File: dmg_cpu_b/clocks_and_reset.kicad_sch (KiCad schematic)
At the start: 112 parts

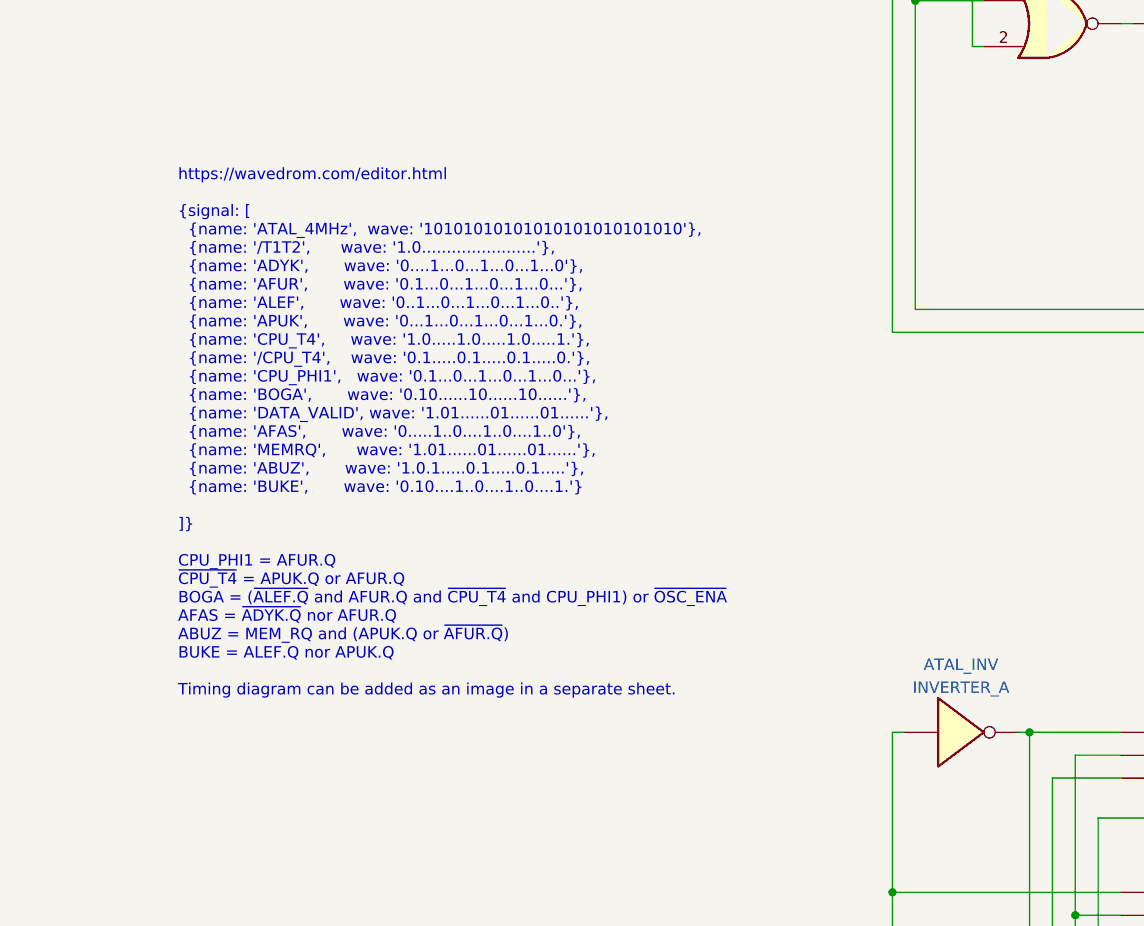
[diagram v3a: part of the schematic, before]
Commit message: Fixed DMA phi2 signal. Notes tidied up, page order modified and draft pdf created for review.
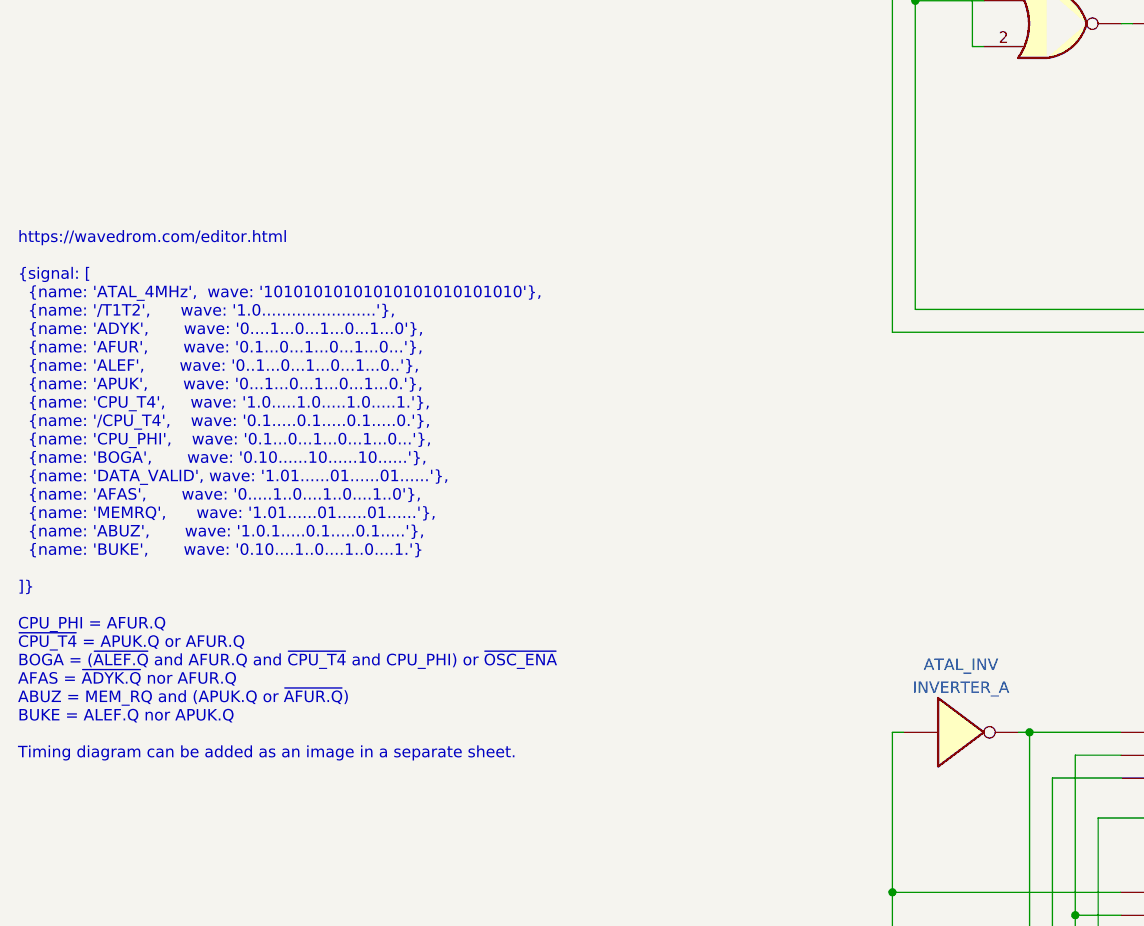
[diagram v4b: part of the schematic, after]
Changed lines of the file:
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@@
   (title_block
     (title "DMG CPU B")
-    (date "2022-05-19")
-    (rev "0")
+    (date "2022-07-08")
+    (rev "0.1")
     (company "CC-BY-SA-4.0 Régis Galland & Michael Singer -- Derived work from Furrtek")
     (comment 1 "https://github.com/msinger/dmg-schematics")
@@
     (effects (font (size 1.27 1.27)) (justify left bottom))
   )
-  (text "https://wavedrom.com/editor.html\n\n{signal: [\n  {name: 'ATAL_4MHz',  wave: '10101010101010101010101010'},\n  {name: '/T1T2',      wave: '1.0.......................'},\n  {name: 'ADYK',       wave: '0....1...0...1...0...1...0'},\n  {name: 'AFUR',       wave: '0.1...0...1...0...1...0...'},\n  {name: 'ALEF',       wave: '0..1...0...1...0...1...0..'},\n  {name: 'APUK',       wave: '0...1...0...1...0...1...0.'},\n  {name: 'CPU_T4',     wave: '1.0.....1.0.....1.0.....1.'},\n  {name: '/CPU_T4',    wave: '0.1.....0.1.....0.1.....0.'},\n  {name: 'CPU_PHI1',   wave: '0.1...0...1...0...1...0...'},\n  {name: 'BOGA',       wave: '0.10......10......10......'},\n  {name: 'DATA_VALID', wave: '1.01......01......01......'},\n  {name: 'AFAS',       wave: '0.....1..0....1..0....1..0'},\n  {name: 'MEMRQ',      wave: '1.01......01......01......'},\n  {name: 'ABUZ',       wave: '1.0.1.....0.1.....0.1.....'},\n  {name: 'BUKE',       wave: '0.10....1..0....1..0....1.'}\n  \n]}\n\nCPU_PHI1 = AFUR.Q\n~{CPU_T4} = APUK.Q or AFUR.Q\nBOGA = (~{ALEF.Q} and AFUR.Q and ~{CPU_T4} and CPU_PHI1) or ~{OSC_ENA} \nAFAS = ~{ADYK.Q} nor AFUR.Q \nABUZ = MEM_RQ and (APUK.Q or ~{AFUR.Q})\nBUKE = ALEF.Q nor APUK.Q\n\nTiming diagram can be added as an image in a separate sheet."
-    (at -62.23 135.255 0)
+  (text "https://wavedrom.com/editor.html\n\n{signal: [\n  {name: 'ATAL_4MHz',  wave: '10101010101010101010101010'},\n  {name: '/T1T2',      wave: '1.0.......................'},\n  {name: 'ADYK',       wave: '0....1...0...1...0...1...0'},\n  {name: 'AFUR',       wave: '0.1...0...1...0...1...0...'},\n  {name: 'ALEF',       wave: '0..1...0...1...0...1...0..'},\n  {name: 'APUK',       wave: '0...1...0...1...0...1...0.'},\n  {name: 'CPU_T4',     wave: '1.0.....1.0.....1.0.....1.'},\n  {name: '/CPU_T4',    wave: '0.1.....0.1.....0.1.....0.'},\n  {name: 'CPU_PHI',    wave: '0.1...0...1...0...1...0...'},\n  {name: 'BOGA',       wave: '0.10......10......10......'},\n  {name: 'DATA_VALID', wave: '1.01......01......01......'},\n  {name: 'AFAS',       wave: '0.....1..0....1..0....1..0'},\n  {name: 'MEMRQ',      wave: '1.01......01......01......'},\n  {name: 'ABUZ',       wave: '1.0.1.....0.1.....0.1.....'},\n  {name: 'BUKE',       wave: '0.10....1..0....1..0....1.'}\n  \n]}\n\nCPU_PHI = AFUR.Q\n~{CPU_T4} = APUK.Q or AFUR.Q\nBOGA = (~{ALEF.Q} and AFUR.Q and ~{CPU_T4} and CPU_PHI) or ~{OSC_ENA} \nAFAS = ~{ADYK.Q} nor AFUR.Q \nABUZ = MEM_RQ and (APUK.Q or ~{AFUR.Q})\nBUKE = ALEF.Q nor APUK.Q\n\nTiming diagram can be added as an image in a separate sheet."
+    (at -80.01 142.24 0)
     (effects (font (size 1.27 1.27)) (justify left bottom))
   )

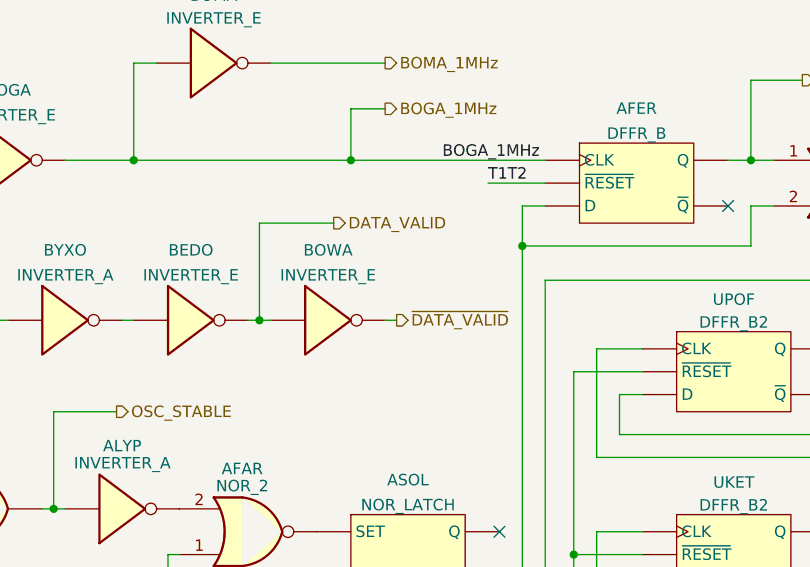
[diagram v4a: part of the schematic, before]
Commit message: Unnecessary comments removed. Data buffers moved to CPU page.
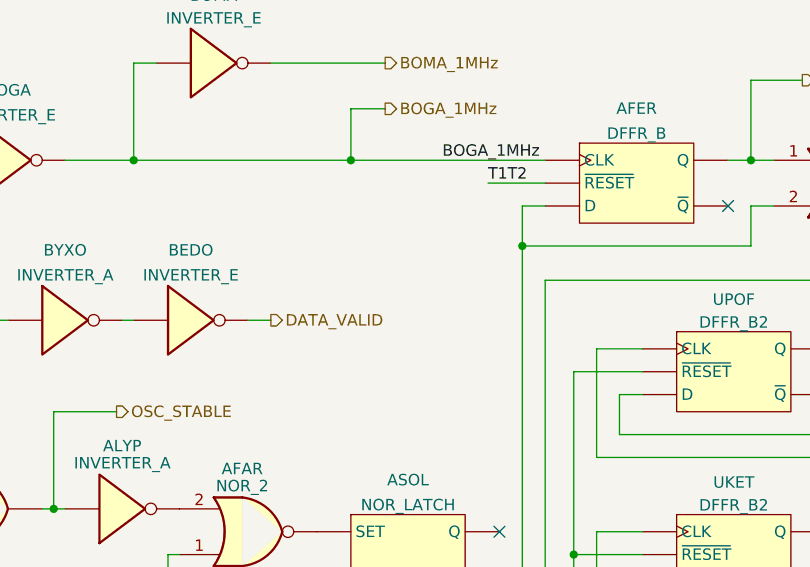
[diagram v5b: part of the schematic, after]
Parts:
- removed BOWA: INVERTER_E, symbol DMG_CPU_Cells:INVERTER_E
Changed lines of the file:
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@@
   (junction (at 113.03 241.3) (diameter 0) (color 0 0 0 0)
-  )
-  (junction (at 269.24 52.705) (diameter 0) (color 0 0 0 0)
   )
   (junction (at 304.165 220.98) (diameter 0) (color 0 0 0 0)
@@
     (stroke (width 0) (type default) (color 0 0 0 0))
   )
-  (wire (pts (xy 269.24 52.705) (xy 269.24 41.91))
-    (stroke (width 0) (type default) (color 0 0 0 0))
-  )
   (wire (pts (xy 190.5 32.385) (xy 187.325 32.385))
     (stroke (width 0) (type default) (color 0 0 0 0))
@@
     (stroke (width 0) (type default) (color 0 0 0 0))
   )
-  (wire (pts (xy 269.24 52.705) (xy 270.51 52.705))
-    (stroke (width 0) (type default) (color 0 0 0 0))
-  )
   (wire (pts (xy 204.47 55.245) (xy 207.01 55.245))
     (stroke (width 0) (type default) (color 0 0 0 0))
@@
     (stroke (width 0) (type default) (color 0 0 0 0))
   )
-  (wire (pts (xy 269.24 41.91) (xy 277.495 41.91))
-    (stroke (width 0) (type default) (color 0 0 0 0))
-  )
   (wire (pts (xy 215.9 104.775) (xy 215.9 116.84))
     (stroke (width 0) (type default) (color 0 0 0 0))
@@
     (stroke (width 0) (type default) (color 0 0 0 0))
   )
-  (wire (pts (xy 283.21 52.705) (xy 284.48 52.705))
-    (stroke (width 0) (type default) (color 0 0 0 0))
-  )
-  (wire (pts (xy 267.97 52.705) (xy 269.24 52.705))
+  (wire (pts (xy 267.97 52.705) (xy 270.51 52.705))
     (stroke (width 0) (type default) (color 0 0 0 0))
   )
@@
     (effects (font (size 1.27 1.27)) (justify left))
   )
-  (hierarchical_label "DATA_VALID" (shape output) (at 277.495 41.91 0)
+  (hierarchical_label "DATA_VALID" (shape output) (at 270.51 52.705 0)
     (effects (font (size 1.27 1.27)) (justify left))
   )
@@
   )
   (hierarchical_label "RAM_CS_EN" (shape output) (at 180.34 161.925 0)
-    (effects (font (size 1.27 1.27)) (justify left))
-  )
-  (hierarchical_label "~{DATA_VALID}" (shape output) (at 284.48 52.705 0)
     (effects (font (size 1.27 1.27)) (justify left))
   )
@@
     (pin "6")
   )
-  (symbol (lib_id "DMG_CPU_Cells:INVERTER_E") (at 276.86 52.705 0) (unit 1)
-    (in_bom yes) (on_board yes) (fields_autoplaced)
-    (property "Reference" "BOWA" (id 0) (at 276.86 44.9285 0))
-    (property "Value" "INVERTER_E" (id 1) (at 276.86 47.7036 0))
-    (property "Footprint" "" (id 2) (at 274.32 52.705 0)
-      (effects (font (size 1.27 1.27)) hide)
-    )
-    (property "Datasheet" "http://iceboy.a-singer.de/doc/dmg_cells.html#inv_e" (id 3) (at 278.13 60.325 0)
-      (effects (font (size 1.27 1.27)) hide)
-    )
-    (pin "1")
-    (pin "2")
-  )
   (symbol (lib_id "DMG_CPU_Cells:DFFR_B2") (at 321.945 220.98 0) (unit 1)

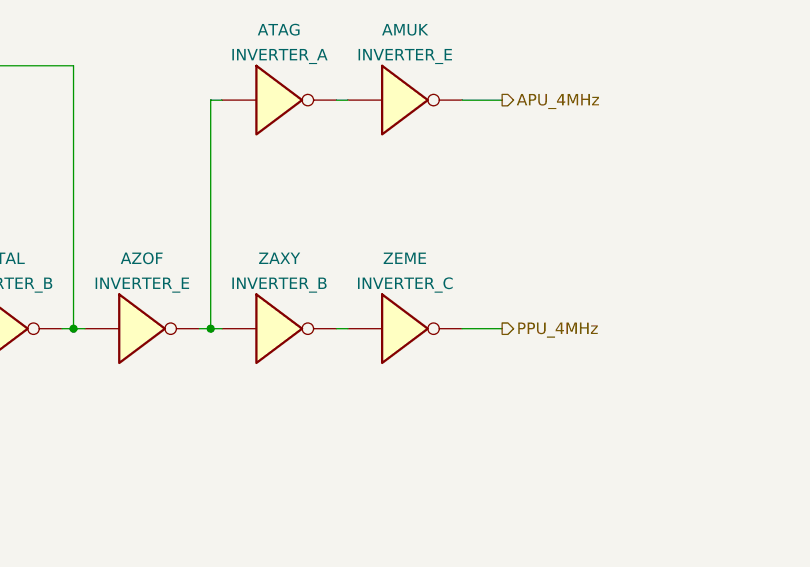
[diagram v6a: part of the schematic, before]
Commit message: Fix done based on github tickets #152 to #155
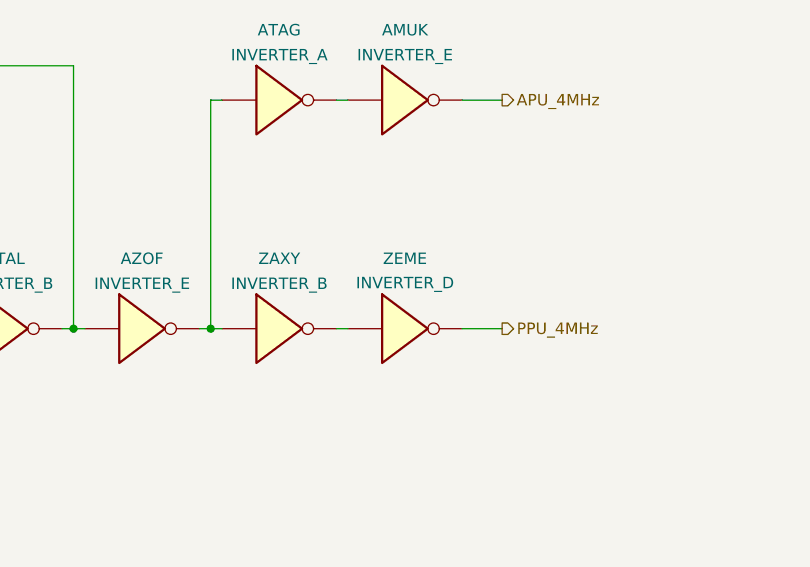
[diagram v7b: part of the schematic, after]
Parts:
- ZEME: value INVERTER_C -> INVERTER_D; symbol DMG_CPU_Cells:INVERTER_C -> DMG_CPU_Cells:INVERTER_D
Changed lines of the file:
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@@
     (pin "1")
   )
-  (symbol (lib_id "DMG_CPU_Cells:INVERTER_C") (at 134.62 241.3 0) (unit 1)
-    (in_bom yes) (on_board yes) (fields_autoplaced)
+  (symbol (lib_id "DMG_CPU_Cells:INVERTER_D") (at 134.62 241.3 0) (unit 1)
+    (in_bom yes) (on_board yes)
     (property "Reference" "ZEME" (id 0) (at 134.62 233.5235 0))
-    (property "Value" "INVERTER_C" (id 1) (at 134.62 236.2986 0))
+    (property "Value" "INVERTER_D" (id 1) (at 134.62 236.22 0))
     (property "Footprint" "" (id 2) (at 132.08 241.3 0)
       (effects (font (size 1.27 1.27)) hide)
     )
-    (property "Datasheet" "http://iceboy.a-singer.de/doc/dmg_cells.html#inv_c" (id 3) (at 135.89 248.92 0)
+    (property "Datasheet" "http://iceboy.a-singer.de/doc/dmg_cells.html#inv_d" (id 3) (at 135.89 248.92 0)
       (effects (font (size 1.27 1.27)) hide)
     )
